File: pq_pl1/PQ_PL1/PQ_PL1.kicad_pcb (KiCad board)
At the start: 2 copper layers, 40 x 40 mm, 9 parts, among them J1 Conn_01x10, J2 Conn_01x10, J3 Conn_01x10, J4 Conn_01x10, U1 PTC06

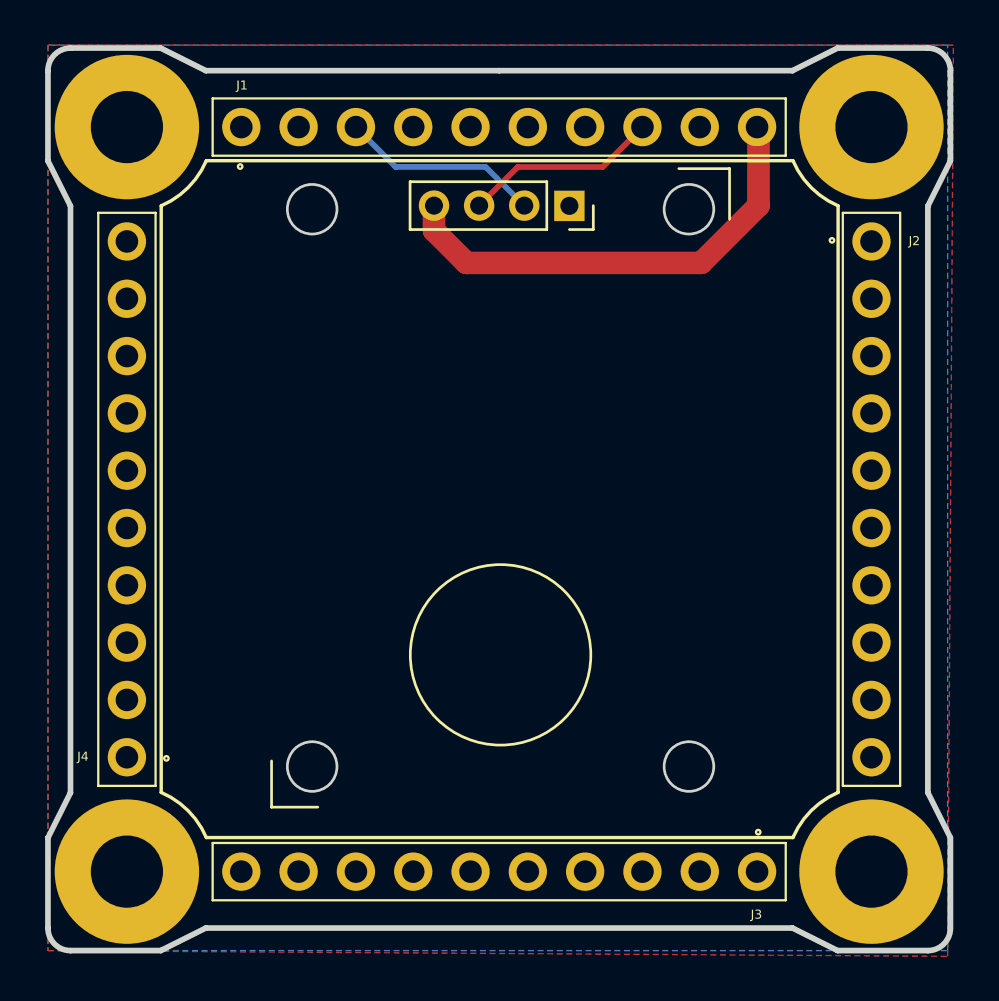
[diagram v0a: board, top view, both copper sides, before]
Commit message: J2(2) pin rename to SWO; DRC, fixed missconnection of VGA power to P/L_power pin instead of the generic 3V3_perm
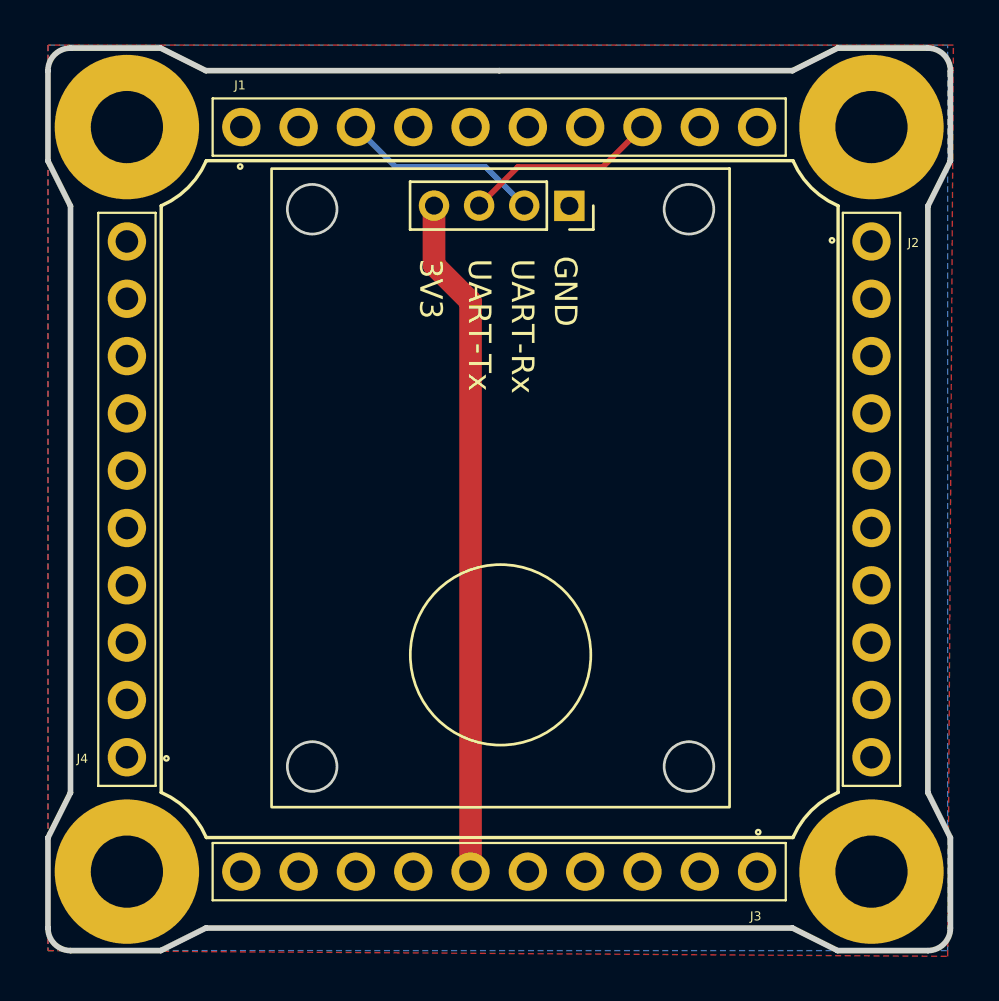
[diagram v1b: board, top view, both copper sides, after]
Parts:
- J1, J2, J3, J4: footprint -nsl_connector:BBL-110-Y-X -> connector-nsl:BBL-110-Y-X
- U1: footprint -nsl_sensor:PTC06 -> sensor-nsl:PTC06
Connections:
- net /STM32_PB3 renamed /SWO
- U1 pad 4: /3V3_PERM -> /P/L_POWER
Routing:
- net /P/L_POWER: track 0.00 -> 30.2 mm
- net /3V3_PERM: track 20.6 -> 0.00 mm
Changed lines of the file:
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@@
   (net 10 "/3V3_PERM")
   (net 11 "/STM32_PA15")
-  (net 12 "/STM32_PB3")
+  (net 12 "/SWO")
   (net 13 "/BATT_NTC")
   (net 14 "/SOLAR_Y")
@@
       (net 1 "GND") (pinfunction "1") (pintype "input"))
   )
-  (footprint "-nsl_connector:BBL-110-Y-X" (layer "F.Cu")
+  (footprint "connector-nsl:BBL-110-Y-X" (layer "F.Cu")
     (at 116.5 38.57 -90)
     (descr "BBL-110-G-E--")
@@
     (property "ki_keywords" "connector")
     (attr through_hole)
-    (fp_text reference "J2" (at -0.02 -1.9 unlocked) (layer "F.SilkS")
-        (effects (font (size 0.4 0.4) (thickness 0.15)))
-    )
-    (fp_text value "Conn_01x10" (at 0 0 90) (layer "F.SilkS") hide
-        (effects (font (size 1.27 1.27) (thickness 0.254)))
-    )
-    (fp_text user "${REFERENCE}" (at 4.2 -3.45 90) (layer "F.Fab")
+    (fp_text reference "J2" (at 0.061 -1.854 unlocked) (layer "F.SilkS")
+        (effects (font (size 0.4 0.4) (thickness 0.15)))
+    )
+    (fp_text value "Conn_01x10" (at 0 0 -90) (layer "F.SilkS") hide
+        (effects (font (size 1.27 1.27) (thickness 0.254)))
+    )
+    (fp_text user "${REFERENCE}" (at 4.2 -3.45 -90) (layer "F.Fab")
         (effects (font (size 1.27 1.27) (thickness 0.254)))
     )
@@
       (net 11 "/STM32_PA15") (pinfunction "Pin_1") (pintype "passive"))
     (pad "2" thru_hole circle (at 2.54 0 270) (size 1.7 1.7) (drill 1) (layers "*.Cu" "*.Mask")
-      (net 12 "/STM32_PB3") (pinfunction "Pin_2") (pintype "passive"))
+      (net 12 "/SWO") (pinfunction "Pin_2") (pintype "passive"))
     (pad "3" thru_hole circle (at 5.08 0 270) (size 1.7 1.7) (drill 1) (layers "*.Cu" "*.Mask")
       (net 13 "/BATT_NTC") (pinfunction "Pin_3") (pintype "passive"))
@@
     )
   )
-  (footprint "-nsl_connector:BBL-110-Y-X" (layer "F.Cu")
+  (footprint "connector-nsl:BBL-110-Y-X" (layer "F.Cu")
     (at 88.57 33.5)
     (descr "BBL-110-G-E--")
@@
     (property "ki_keywords" "connector")
     (attr through_hole)
-    (fp_text reference "J1" (at 0.03 -1.85 unlocked) (layer "F.SilkS")
+    (fp_text reference "J1" (at -0.061 -1.854 unlocked) (layer "F.SilkS")
         (effects (font (size 0.4 0.4) (thickness 0.15)))
     )
@@
         (effects (font (size 1.27 1.27) (thickness 0.254)))
     )
-    (fp_text user "${REFERENCE}" (at 3.78 0.4) (layer "F.Fab")
+    (fp_text user "${REFERENCE}" (at 4.2 -3.45) (layer "F.Fab")
         (effects (font (size 1.27 1.27) (thickness 0.254)))
     )
@@
     )
   )
-  (footprint "-nsl_connector:BBL-110-Y-X" (layer "F.Cu")
+  (footprint "connector-nsl:BBL-110-Y-X" (layer "F.Cu")
     (at 83.5 61.43 90)
     (descr "BBL-110-G-E--")
@@
     (property "ki_keywords" "connector")
     (attr through_hole)
-    (fp_text reference "J4" (at 0.03 -1.95 unlocked) (layer "F.SilkS")
+    (fp_text reference "J4" (at -0.061 -1.976 unlocked) (layer "F.SilkS")
         (effects (font (size 0.4 0.4) (thickness 0.15)))
     )
@@
         (effects (font (size 1.27 1.27) (thickness 0.254)))
     )
-    (fp_text user "${REFERENCE}" (at 11.5824 1.8288) (layer "F.Fab") hide
+    (fp_text user "${REFERENCE}" (at 4.2 -3.45 90) (layer "F.Fab")
         (effects (font (size 1.27 1.27) (thickness 0.254)))
     )
@@
       (net 1 "GND") (pinfunction "1") (pintype "input"))
   )
-  (footprint "-nsl_sensor:PTC06" (layer "F.Cu")
+  (footprint "sensor-nsl:PTC06" (layer "F.Cu")
     (at 100.0608 49.492 -90)
     (property "Sheetfile" "PQ_PL1.kicad_sch")
     (property "Sheetname" "")
     (attr through_hole)
-    (fp_text reference "U1" (at 14.478 0 unlocked) (layer "F.SilkS") hide
-        (effects (font (size 0.4 0.4) (thickness 0.15)))
-    )
-    (fp_text value "PTC06" (at 0.3556 0.2032 -90 unlocked) (layer "F.Fab")
-        (effects (font (size 1 1) (thickness 0.15)))
+    (fp_text reference "U1" (at 0.4155 -5.08 -90 unlocked) (layer "F.SilkS") hide
+        (effects (font (size 0.4 0.4) (thickness 0.1)))
+    )
+    (fp_text value "PTC06" (at 0.188 -3.6882 -90 unlocked) (layer "F.Fab")
+        (effects (font (size 1 1) (thickness 0.15)))
+    )
+    (fp_text user "3V3" (at -10.16 3.683 -90 unlocked) (layer "F.SilkS")
+        (effects (font (size 1 1) (thickness 0.15)) (justify left bottom))
+    )
+    (fp_text user "UART-Rx" (at -10.16 -0.381 -90 unlocked) (layer "F.SilkS")
+        (effects (font (size 1 1) (thickness 0.15)) (justify left bottom))
+    )
+    (fp_text user "GND" (at -10.287 -2.286 -90 unlocked) (layer "F.SilkS")
+        (effects (font (size 1 1) (thickness 0.15)) (justify left bottom))
+    )
+    (fp_text user "UART-Tx" (at -10.16 1.524 -90 unlocked) (layer "F.SilkS")
+        (effects (font (size 1 1) (thickness 0.15)) (justify left bottom))
     )
     (fp_text user "${REFERENCE}" (at -12.51 -0.05) (layer "F.Fab")
         (effects (font (size 1 1) (thickness 0.15)))
     )
-    (fp_text user "${REFERENCE}" (at 20.8788 9.2724 -90 unlocked) (layer "F.Fab")
-        (effects (font (size 1 1) (thickness 0.15)))
-    )
-    (fp_line (start -14.15 -10.15) (end -14.15 -7.9)
-      (stroke (width 0.12) (type solid)) (layer "F.SilkS"))
-    (fp_line (start -14.15 -10.15) (end -11.9 -10.15)
-      (stroke (width 0.12) (type solid)) (layer "F.SilkS"))
+    (fp_text user "${REFERENCE}" (at 0.061 -5.0852 -90 unlocked) (layer "F.Fab")
+        (effects (font (size 1 1) (thickness 0.15)))
+    )
+    (fp_text_box "PTC06 Camera Module"
+    (start -2.569 5.08) (end 3.4 -5.08) (angle 90) (layer "F.SilkS")
+        (effects (font (size 1 1) (thickness 0.15)) (justify top))
+    )
     (fp_line (start -13.57 -2.05) (end -13.57 4.01)
       (stroke (width 0.12) (type solid)) (layer "F.SilkS"))
@@
     (fp_line (start -11.45 -2.05) (end -11.45 4.01)
       (stroke (width 0.12) (type solid)) (layer "F.SilkS"))
-    (fp_line (start 14.15 10.15) (end 12.1 10.15)
-      (stroke (width 0.12) (type solid)) (layer "F.SilkS"))
-    (fp_line (start 14.15 10.15) (end 14.15 8.1)
-      (stroke (width 0.12) (type solid)) (layer "F.SilkS"))
+    (fp_rect (start -14.15 -10.15) (end 14.15 10.15)
+      (stroke (width 0.12) (type default)) (fill none) (layer "F.SilkS"))
     (fp_circle (center 7.4 0) (end 11.4 0)
       (stroke (width 0.12) (type solid)) (fill none) (layer "F.SilkS"))
@@
       (stroke (width 0.1) (type solid)) (layer "F.Fab"))
     (pad "1" thru_hole rect (at -12.5 -3.05 270) (size 1.35 1.35) (drill 0.8) (layers "*.Cu" "*.Mask")
-      (net 1 "GND") (pinfunction "GND") (pintype "power_out") (zone_connect 2))
+      (net 1 "GND") (pinfunction "GND") (pintype "power_out"))
     (pad "2" thru_hole oval (at -12.51 -1.05 270) (size 1.35 1.35) (drill 0.8) (layers "*.Cu" "*.Mask")
       (net 4 "/UART_RX") (pinfunction "RX") (pintype "input"))
@@
       (net 9 "/UART_TX") (pinfunction "TX") (pintype "output"))
     (pad "4" thru_hole oval (at -12.51 2.95 270) (size 1.35 1.35) (drill 0.8) (layers "*.Cu" "*.Mask")
-      (net 10 "/3V3_PERM") (pinfunction "3V3") (pintype "power_in"))
+      (net 24 "/P{slash}L_POWER") (pinfunction "3V3") (pintype "power_in"))
     (model "${KICAD_NSL_DIR}/sensor-nsl/StepFiles/Camera module - PTC06 .step"
       (offset (xyz 34 10 2))
@@
     )
   )
-  (footprint "-nsl_connector:BBL-110-Y-X" (layer "F.Cu")
+  (footprint "connector-nsl:BBL-110-Y-X" (layer "F.Cu")
     (at 111.43 66.5 180)
     (descr "BBL-110-G-E--")
@@
     (property "ki_keywords" "connector")
     (attr through_hole)
-    (fp_text reference "J3" (at 0.03 -1.9 unlocked) (layer "F.SilkS")
-        (effects (font (size 0.4 0.4) (thickness 0.15)))
-    )
-    (fp_text value "Conn_01x10" (at 0 0) (layer "F.SilkS") hide
-        (effects (font (size 1.27 1.27) (thickness 0.254)))
-    )
-    (fp_text user "${REFERENCE}" (at 4.2 -3.45) (layer "F.Fab") hide
+    (fp_text reference "J3" (at 0.061 -1.976 unlocked) (layer "F.SilkS")
+        (effects (font (size 0.4 0.4) (thickness 0.15)))
+    )
+    (fp_text value "Conn_01x10" (at 0 0 180) (layer "F.SilkS") hide
+        (effects (font (size 1.27 1.27) (thickness 0.254)))
+    )
+    (fp_text user "${REFERENCE}" (at 4.2 -3.45 180) (layer "F.Fab")
         (effects (font (size 1.27 1.27) (thickness 0.254)))
     )
@@
   (segment (start 100.8248 35.268) (end 104.5912 35.268) (width 0.25) (layer "F.Cu") (net 9))
   (segment (start 99.1108 36.982) (end 100.8248 35.268) (width 0.25) (layer "F.Cu") (net 9))
-  (segment (start 111.496 36.98) (end 111.496 33.566) (width 1) (layer "F.Cu") (net 10))
-  (segment (start 108.956 39.52) (end 111.496 36.98) (width 1) (layer "F.Cu") (net 10))
-  (segment (start 97.1108 36.982) (end 97.1108 38.0888) (width 1) (layer "F.Cu") (net 10))
-  (segment (start 97.1108 38.0888) (end 98.542 39.52) (width 1) (layer "F.Cu") (net 10))
-  (segment (start 111.496 33.566) (end 111.43 33.5) (width 1) (layer "F.Cu") (net 10))
-  (segment (start 98.542 39.52) (end 108.956 39.52) (width 1) (layer "F.Cu") (net 10))
+  (segment (start 97.1108 36.982) (end 97.1108 39.6128) (width 1) (layer "F.Cu") (net 24))
+  (segment (start 98.73 41.232) (end 98.73 66.5) (width 1) (layer "F.Cu") (net 24))
+  (segment (start 97.1108 39.6128) (end 98.73 41.232) (width 1) (layer "F.Cu") (net 24))
   (zone (net 1) (net_name "GND") (layer "F.Cu") (hatch edge 0.5)
     (connect_pads (clearance 0.5))
